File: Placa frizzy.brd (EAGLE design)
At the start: 68.6 x 53.3 mm, 86 parts, among them IC2 LM358D, Q1 2N7002PW, Q4 FDN340P, Q5 FDN340P, U1 FTS31XS-U, U2 AMS1117-3.3, U4 ATMEGA328P_TQFP, Y1 16MHZ

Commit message: Ultima version mandada a fabrica
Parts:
- moved R5 1.42 mm to (111.4, 58.4)
- moved R6 1.31 mm to (109.2, 58.4)
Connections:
- removed net VCC: C12.1, C13.1, C14.1, JP1.2, JP10.2, JP11.2, JP12.2, JP13.2, JP14.2, JP15.2, JP16.2, JP17.2, JP18.2, JP20.2, JP21.2, JP22.2, JP23.2, JP24.2, JP25.2, JP26.2, JP5.2, JP6.2, JP7.2, JP8.2, JP9.2, R3.2, R8.2, U4.18, U4.4, U4.6
- net 5V: now also C12.1, C13.1, C14.1, JP1.2, JP10.2, JP11.2, JP12.2, JP13.2, JP14.2, JP15.2, JP16.2, JP17.2, JP18.2, JP20.2, JP21.2, JP22.2, JP23.2, JP24.2, JP25.2, JP26.2, JP5.2, JP6.2, JP7.2, JP8.2, JP9.2, R3.2, R8.2, U4.18, U4.4, U4.6
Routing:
- net VCC: track 128.2 -> 0.00 mm, vias 1 -> 0
- net 5V: track 157.0 -> 276.6 mm, vias 3 -> 5
- net RX: track 37.4 -> 39.3 mm
- net TX: track 33.9 -> 35.5 mm
- net AREF: track 71.6 -> 70.7 mm
- net 3.3V: track 121.9 -> 122.6 mm
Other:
- outline, holes or cut-outs redrawn
- board text added: "."
- board text added: "0"
- board text added: "1"

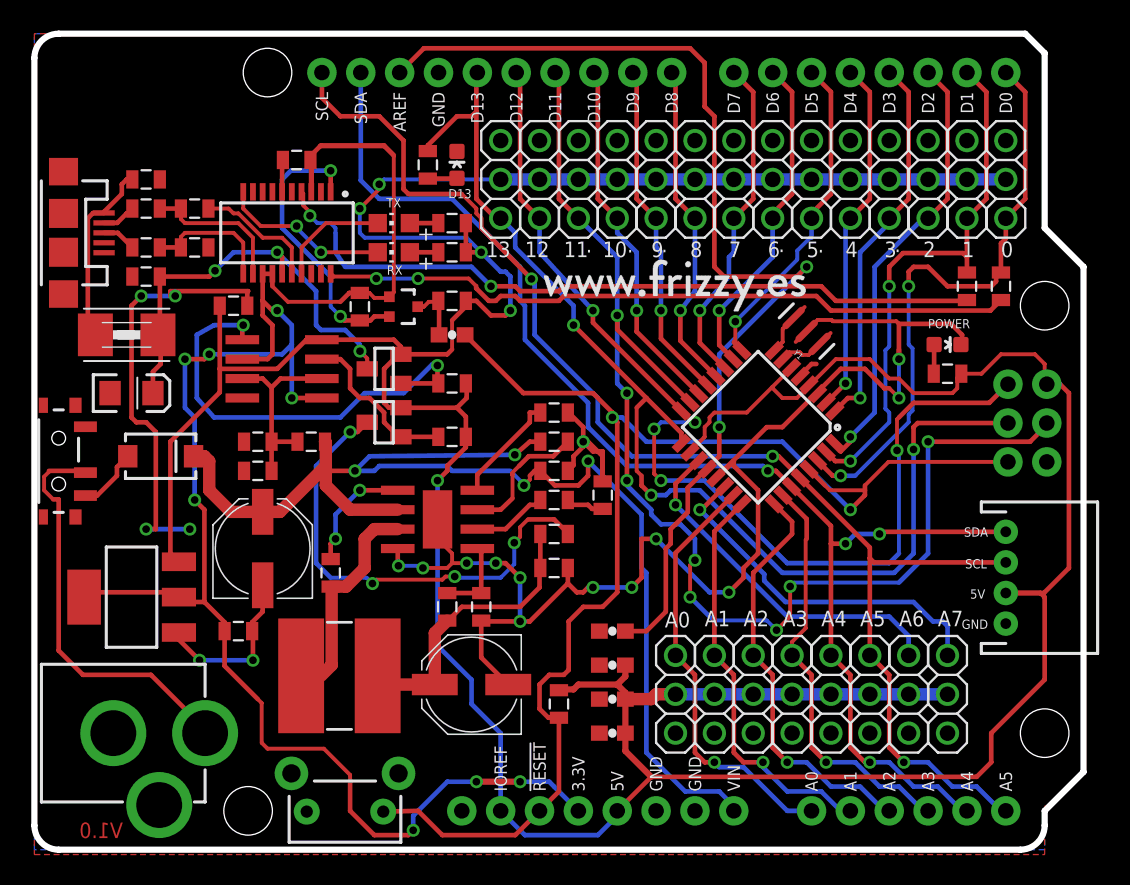
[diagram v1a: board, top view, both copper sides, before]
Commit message: Vias Tapadas, USB cambiado, TX RX añadido
se ha reparado tambien la alimentacion de 5V
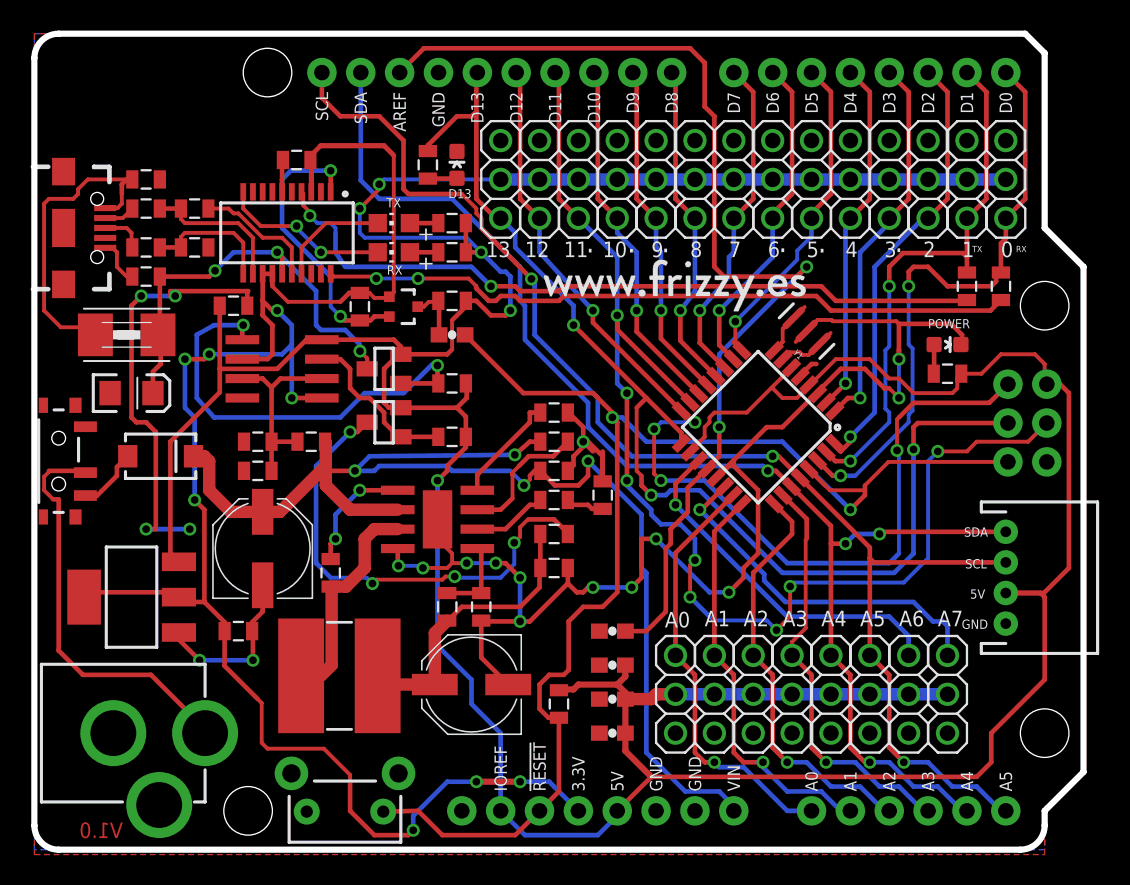
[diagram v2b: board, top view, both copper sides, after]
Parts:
- removed JP2: USB, SparkFun-Connectors:USB-MICROB
- added JP4: (no value), SparkFun-Connectors:USB-B-MICRO-SMD_V03
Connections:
- net GND: now also JP4.GND1, JP4.SHIELD1, JP4.SHIELD2, JP4.SHIELD3; no longer JP2.GND, JP2.MT1, JP2.MT2
- net N$24: now also JP4.D-1; no longer JP2.D-
- net N$28: now also JP4.D+1; no longer JP2.D+
- net N$29: now also JP4.VBUS1; no longer JP2.VBUS
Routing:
- net N$29: track 12.2 -> 20.9 mm
- net GND: track 150.7 -> 153.2 mm
- net MOSI/PIN11: track 81.9 -> 81.3 mm
- net N$28: track 2.24 -> 2.83 mm
